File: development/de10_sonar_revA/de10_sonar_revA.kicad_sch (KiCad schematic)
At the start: 11 parts, among them U1 TUSS4470

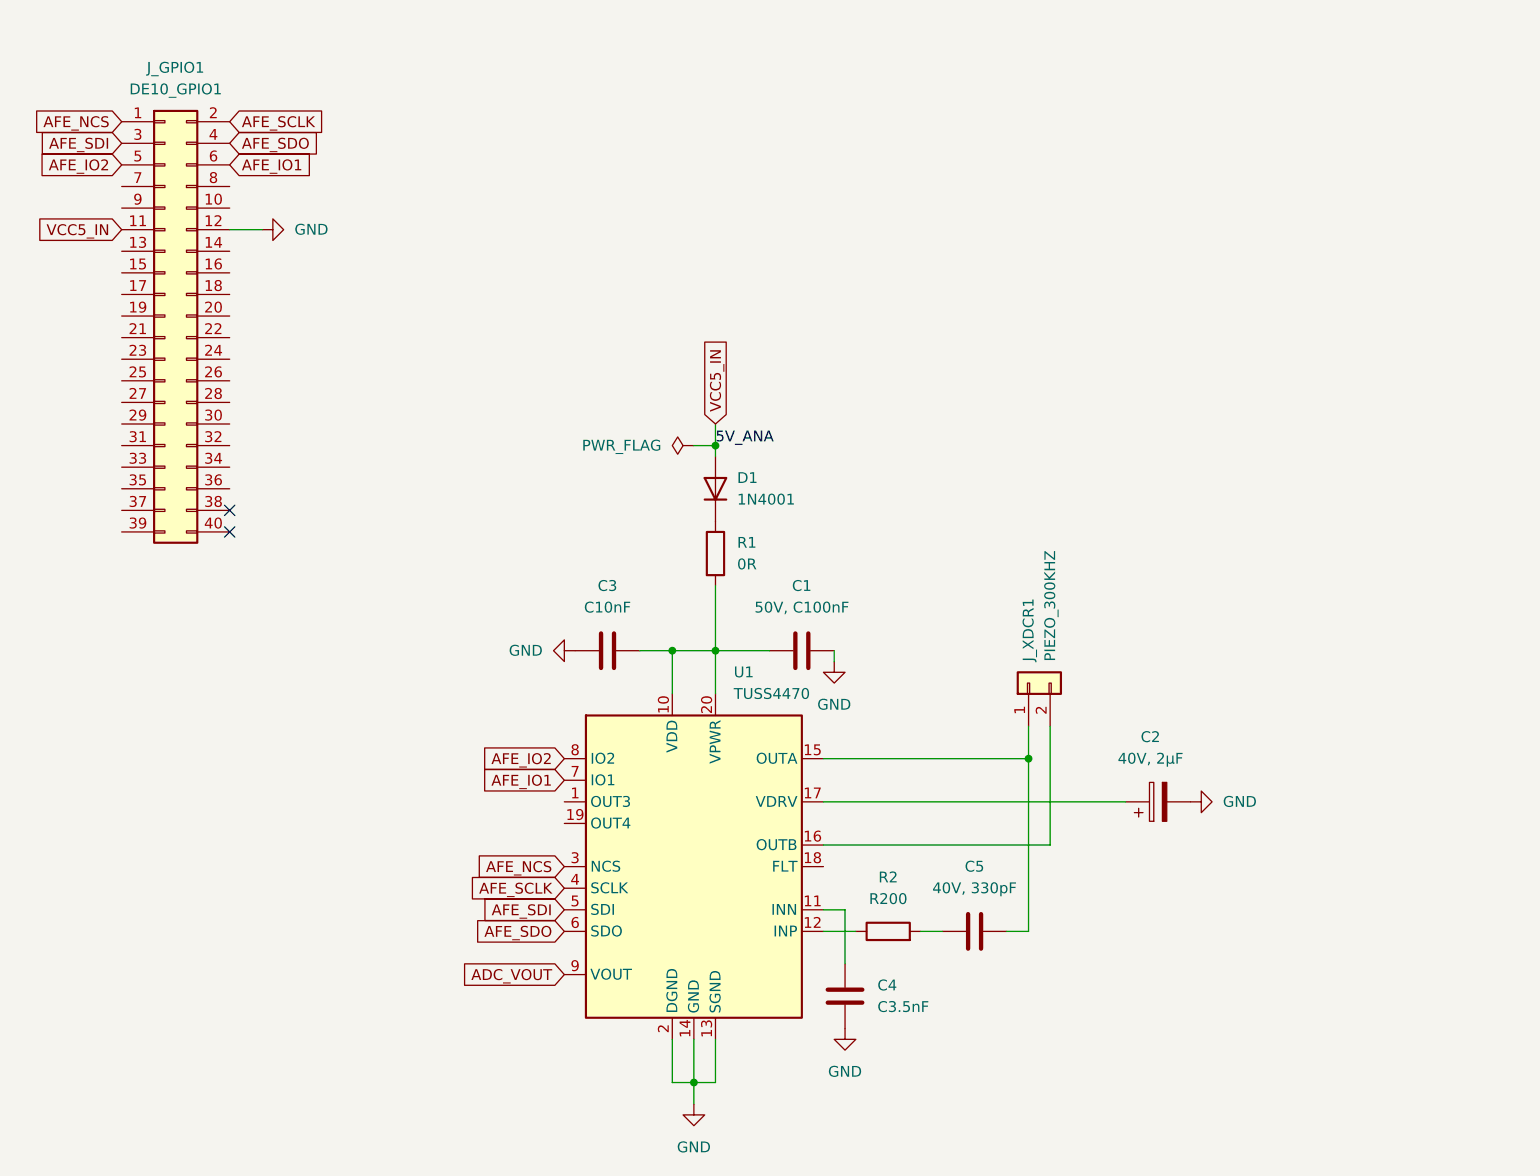
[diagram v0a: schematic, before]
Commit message: Added ads805e symbol and footprint as well as continued the schematic
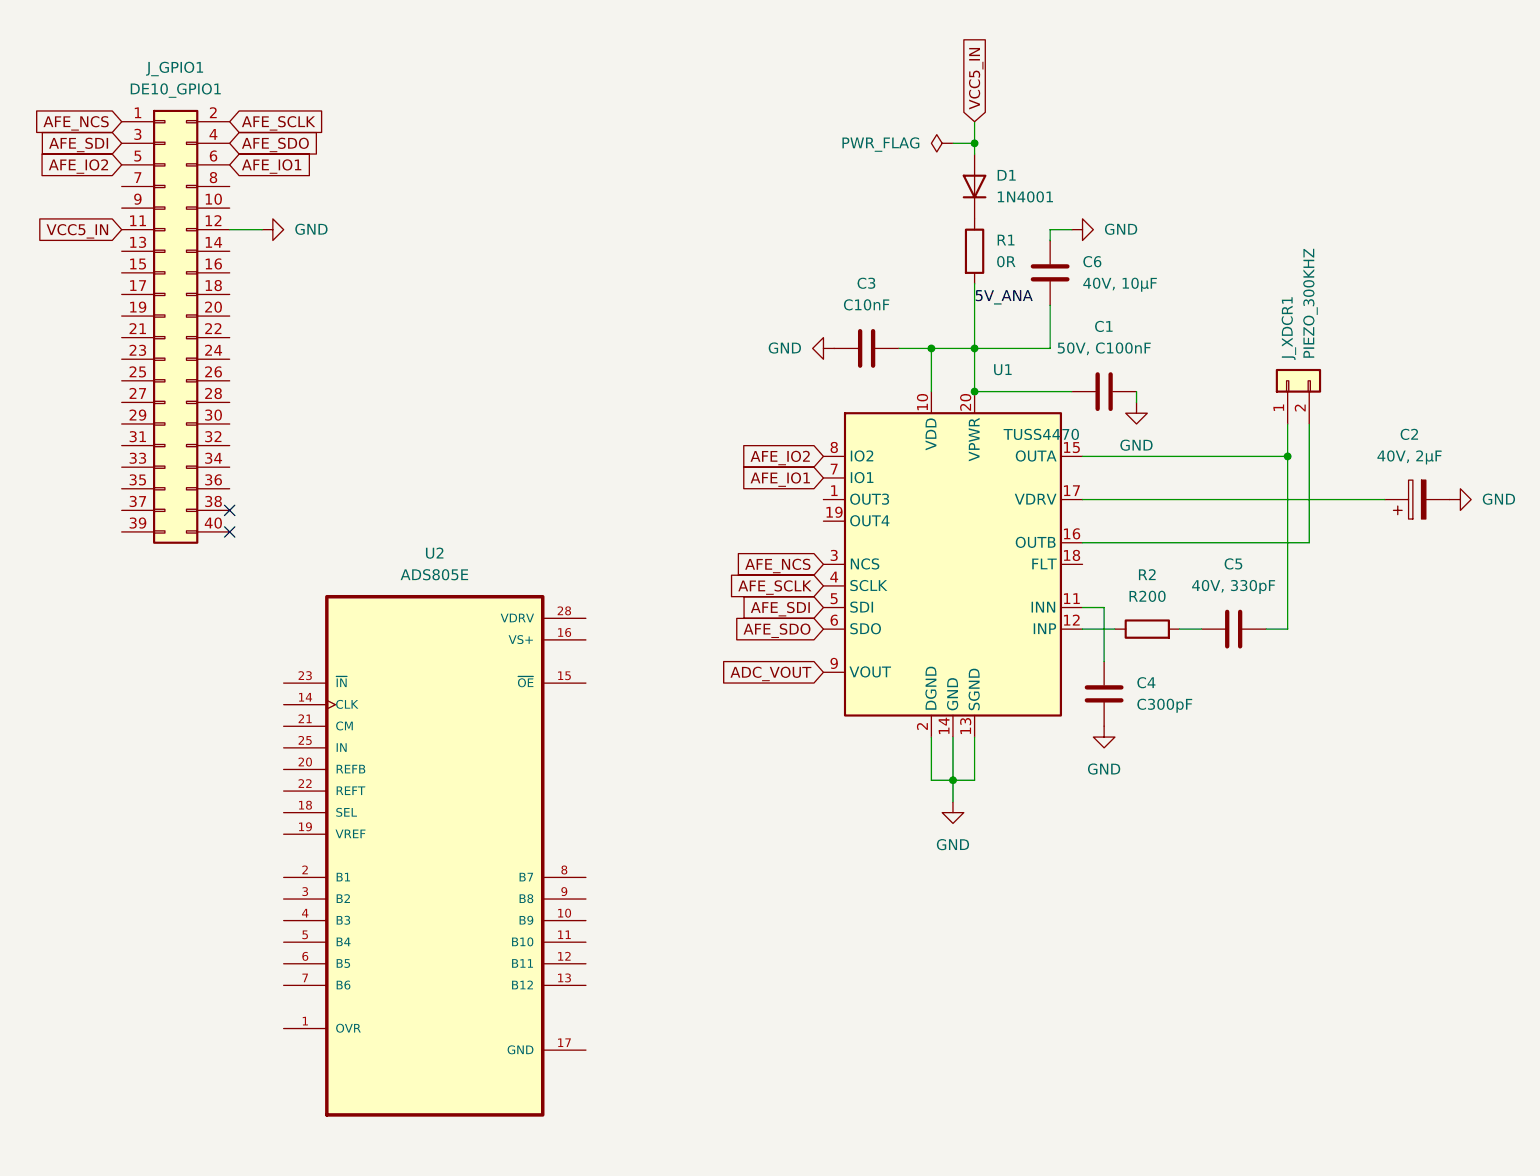
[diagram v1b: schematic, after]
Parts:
- added C6: 40V, 10µF, Capacitor_SMD:C_0603_1608Metric, symbol Device:C
- added U2: ADS805E, ADS805E:SOP65P780X200-28N, symbol ADS805E:ADS805E
- C4: value C3.5nF -> C300pF
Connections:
- net GND: now also C6.2, U2.17 (GND), U2.24 (GND), U2.26 (GND)
- net 5V_ANA: now reaches C1.1, C3.1, R1.2, U1.10 (VDD), U1.20 (VPWR)
- net 5V_ANA: now also C6.1
- new net VS+: U2.16 (VS+), U2.27 (VS+)
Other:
- moved on the sheet: C1, C2, C3, C4, C5, D1, J_XDCR1, R1, R2, U1

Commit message: Continued schematic work with TUSS4470 and ADS805 hookup
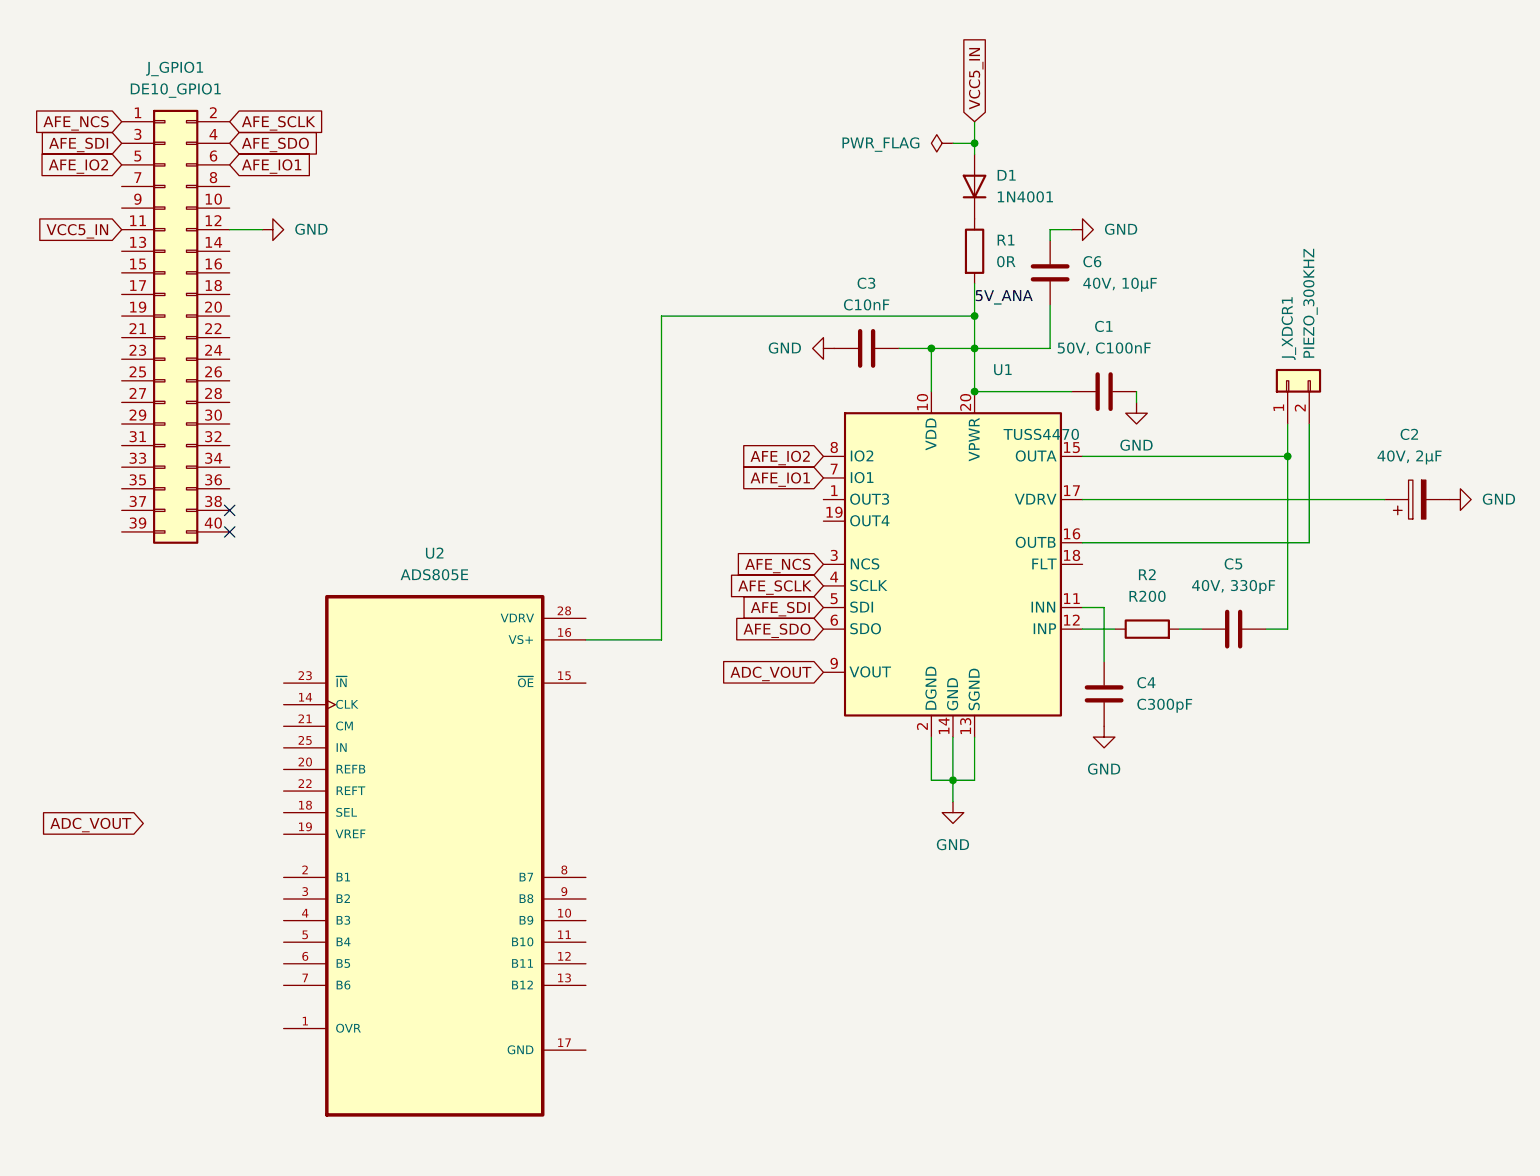
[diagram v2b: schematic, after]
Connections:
- net 5V_ANA is gone; now on net VS+: C1.1, C3.1, C6.1, R1.2, U1.10 (VDD), U1.20 (VPWR)
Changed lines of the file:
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@@
+	)
+	(junction
+		(at 125.73 52.07)
+		(diameter 0)
+		(color 0 0 0 0)
 	)
 	(junction
@@
 	(wire
 		(pts
+			(xy 88.9 52.07) (xy 88.9 90.17)
+		)
+		(stroke
+			(width 0)
+			(type default)
+		)
+	)
+	(wire
+		(pts
+			(xy 125.73 52.07) (xy 125.73 55.88)
+		)
+		(stroke
+			(width 0)
+			(type default)
+		)
+	)
+	(wire
+		(pts
 			(xy 138.43 68.58) (xy 162.56 68.58)
 		)
@@
 	(wire
 		(pts
+			(xy 88.9 90.17) (xy 80.01 90.17)
+		)
+		(stroke
+			(width 0)
+			(type default)
+		)
+	)
+	(wire
+		(pts
 			(xy 165.1 64.77) (xy 165.1 78.74)
 		)
@@
 	(wire
 		(pts
-			(xy 125.73 48.26) (xy 125.73 55.88)
+			(xy 125.73 48.26) (xy 125.73 52.07)
 		)
 		(stroke
@@
 		(pts
 			(xy 125.73 55.88) (xy 134.62 55.88)
+		)
+		(stroke
+			(width 0)
+			(type default)
+		)
+	)
+	(wire
+		(pts
+			(xy 125.73 52.07) (xy 88.9 52.07)
 		)
 		(stroke
@@
 			(effects
 				(font
+					(size 1.27 1.27)
+				)
+				(justify left)
+				(hide yes)
+			)
+		)
+	)
+	(global_label "ADC_VOUT"
+		(shape input)
+		(at 27.94 111.76 180)
+		(fields_autoplaced yes)
+		(effects
+			(font
+				(size 1.27 1.27)
+			)
+			(justify right)
+		)
+		(property "Intersheetrefs" "${INTERSHEET_REFS}"
+			(at 39.9966 111.76 0)
+			(effects
+				(font
